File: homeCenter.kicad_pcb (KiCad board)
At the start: 2 copper layers, 59.7 x 57.1 mm, 45 parts, among them J1 sensor, J2 sensor, J3 mcu_en, J4 Conn_01x01_Male, P1 USB_C_Plug_USB2.0, Q1 S8050, U1 AMS1117-3.3, U2 ESP32-WROOM-32, U3 FengNiaoR3

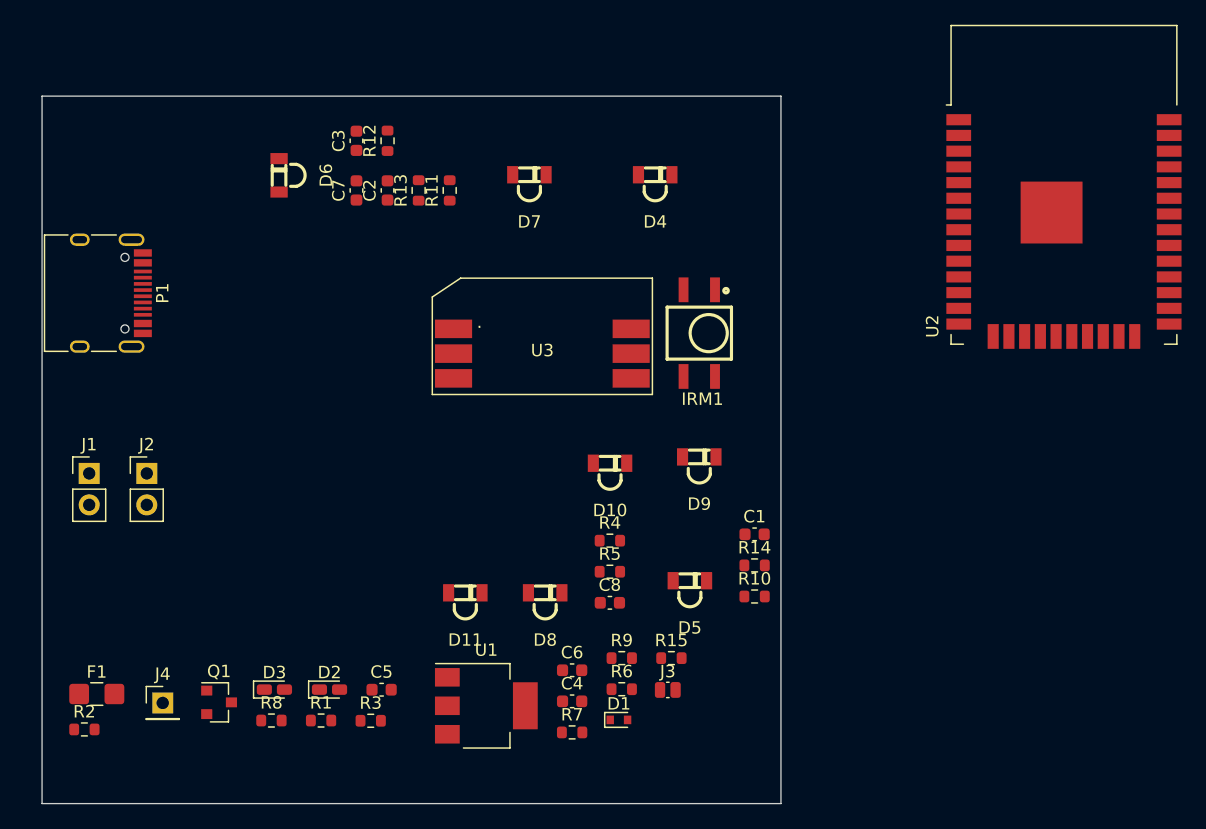
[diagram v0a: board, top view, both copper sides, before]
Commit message: convert to kicad 4.99
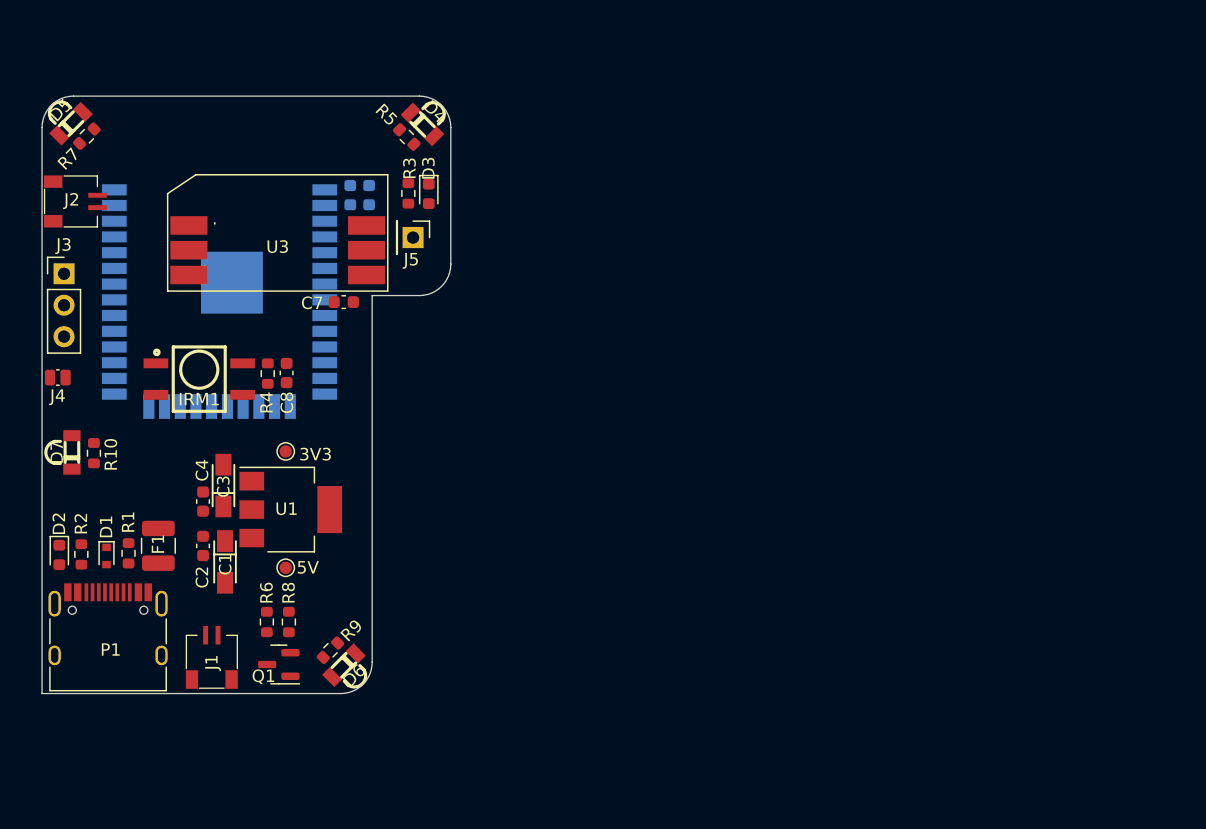
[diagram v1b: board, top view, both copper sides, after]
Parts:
- removed D10, D11, D8, D9: IR, kay:LED-SMD_L3.0-W2.7-RD
- removed R11: 1k, Resistor_SMD:R_0603_1608Metric
- removed R12, R14, R15: 47, Resistor_SMD:R_0603_1608Metric
- removed R13: 100k, Resistor_SMD:R_0603_1608Metric
- added 3V3: 3V3, TestPoint:TestPoint_Pad_D1.0mm, F.Cu at (45.1, 54.1)
- added 5V: 5V, TestPoint:TestPoint_Pad_D1.0mm, F.Cu at (45.1, 63.5)
- added J5: Conn_01x01_Male, kay:433M_ANT, F.Cu at (55.4, 36.8)
- C1, C3: footprint Capacitor_SMD:C_0603_1608Metric -> kay:CAP-SMD_L3.2-W1.6-RD
- C5, C6, U2: moved to B.Cu
- D2: value LED -> POWER; footprint LED_SMD:LED_0603_1608Metric_Castellated -> LED_SMD:LED_0603_1608Metric
- D3: value LED -> TEST; footprint LED_SMD:LED_0603_1608Metric_Castellated -> LED_SMD:LED_0603_1608Metric
- F1: footprint Fuse:Fuse_1206_3216Metric_Castellated -> Fuse:Fuse_1210_3225Metric
- J1, J2: footprint Connector_PinHeader_2.54mm:PinHeader_1x02_P2.54mm_Vertical -> kay:SH1.0MM-SMD
- J3: value mcu_en -> M_SERIAL; footprint Capacitor_SMD:C_0504_1310Metric_Pad0.83x1.28mm_HandSolder -> Connector_PinHeader_2.54mm:PinHeader_1x03_P2.54mm_Vertical
- J4: value Conn_01x01_Male -> mcu_en; footprint Connector_PinHeader_2.54mm:PinHeader_1x01_P2.54mm_Vertical -> Capacitor_SMD:C_0504_1310Metric_Pad0.83x1.28mm_HandSolder
- R1: value 51k -> NC/0
- R2: value NC/0 -> 47K
- R4: value 47K -> 100
- R5: value 100 -> 47
- R6: value 47 -> 1k
- R8: value 47 -> 100k
- moved U2 68.4 mm to (39.7, 41.2), turned to 180 degrees
- moved D5 62.1 mm to (27.7, 27.6), turned to -135 degrees
- moved R7 62.1 mm to (29.0, 28.6), turned to 45 degrees
- moved J3 59.2 mm to (27.2, 39.8)
- moved R10 54.6 mm to (29.6, 54.2), turned to 90 degrees
- moved D1 43.5 mm to (30.6, 62.5), turned to -90 degrees
- moved D7 43.2 mm to (27.8, 54.2), turned to -90 degrees
- moved C1 42.8 mm to (40.2, 63.0), turned to 90 degrees
- moved R3 42.7 mm to (55.0, 33.3), turned to 90 degrees
- moved C6 42.4 mm to (50.3, 33.4), turned to 90 degrees
- moved D3 41.9 mm to (56.6, 33.3), turned to -90 degrees
- moved IRM1 40.6 mm to (38.1, 48.3), turned to 90 degrees
- moved C5 40.0 mm to (51.8, 33.4), turned to 90 degrees
- moved D6 39.9 mm to (49.8, 71.4), turned to 45 degrees
- moved R5 38.8 mm to (54.9, 28.7), turned to -45 degrees
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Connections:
- J3 pad 1: /MCU_IO0 -> GND
- J3 pad 2: GND -> /MCU_RX0
- J4 pad 1: Net-(J4-Pad1) -> /MCU_IO0
- P1 pad A5: Net-(P1-PadA5) -> unconnected-(P1-PadA5)
- P1 pad A6: Net-(P1-PadA6) -> unconnected-(P1-PadA6)
- P1 pad A7: Net-(P1-PadA7) -> unconnected-(P1-PadA7)
- P1 pad B5: Net-(P1-PadA5) -> unconnected-(P1-PadB5)
- R1 pad 1: GND -> VCC
- R1 pad 2: Net-(P1-PadA5) -> Net-(F1-Pad2)
- R10 pad 1: Net-(D8-Pad2) -> Net-(D7-Pad2)
- R2 pad 1: VCC -> 3V3
- R2 pad 2: Net-(F1-Pad2) -> Net-(D2-Pad2)
- R3 pad 1: 3V3 -> Net-(D3-Pad2)
- R3 pad 2: Net-(D2-Pad2) -> 3V3
- R4 pad 1: Net-(D3-Pad2) -> Net-(C8-Pad1)
- R5 pad 1: Net-(C8-Pad1) -> Net-(D4-Pad2)
- R6 pad 1: Net-(D4-Pad2) -> /IR_TX0
- R6 pad 2: 3V3 -> Net-(Q1-Pad2)
- R8 pad 1: Net-(D6-Pad2) -> GND
- R8 pad 2: 3V3 -> Net-(Q1-Pad2)
- R9 pad 1: Net-(D7-Pad2) -> Net-(D6-Pad2)
- U2 pad 10: Net-(U2-Pad10) -> unconnected-(U2-Pad10)
- U2 pad 11: Net-(U2-Pad11) -> unconnected-(U2-Pad11)
- U2 pad 12: Net-(U2-Pad12) -> unconnected-(U2-Pad12)
- U2 pad 17: Net-(U2-Pad17) -> unconnected-(U2-Pad17)
- U2 pad 18: Net-(U2-Pad18) -> unconnected-(U2-Pad18)
- U2 pad 19: Net-(U2-Pad19) -> unconnected-(U2-Pad19)
- U2 pad 20: Net-(U2-Pad20) -> unconnected-(U2-Pad20)
- U2 pad 21: Net-(U2-Pad21) -> unconnected-(U2-Pad21)
- U2 pad 22: Net-(U2-Pad22) -> unconnected-(U2-Pad22)
- U2 pad 24: Net-(U2-Pad24) -> unconnected-(U2-Pad24)
- U2 pad 26: Net-(U2-Pad26) -> unconnected-(U2-Pad26)
- U2 pad 28: Net-(U2-Pad28) -> unconnected-(U2-Pad28)
- U2 pad 29: Net-(U2-Pad29) -> unconnected-(U2-Pad29)
- U2 pad 30: Net-(U2-Pad30) -> unconnected-(U2-Pad30)
- U2 pad 31: Net-(U2-Pad31) -> unconnected-(U2-Pad31)
- U2 pad 32: Net-(U2-Pad32) -> unconnected-(U2-Pad32)
- U2 pad 33: Net-(U2-Pad33) -> unconnected-(U2-Pad33)
- U2 pad 36: Net-(U2-Pad36) -> unconnected-(U2-Pad36)
- U2 pad 37: Net-(U2-Pad37) -> unconnected-(U2-Pad37)
- U2 pad 4: Net-(U2-Pad4) -> unconnected-(U2-Pad4)
- U2 pad 5: Net-(U2-Pad5) -> unconnected-(U2-Pad5)
- U2 pad 6: Net-(U2-Pad6) -> unconnected-(U2-Pad6)
- U2 pad 7: Net-(U2-Pad7) -> unconnected-(U2-Pad7)
- U2 pad 8: Net-(U2-Pad8) -> unconnected-(U2-Pad8)
- U2 pad 9: Net-(U2-Pad9) -> unconnected-(U2-Pad9)
- U3 pad 5: Net-(J4-Pad1) -> Net-(J5-Pad1)
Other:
- board size 59.7 x 57.1 mm -> 33 x 48.3 mm
- net class Default removed

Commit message: pcb
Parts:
- Q1: value S8050 -> Q_NPN_BEC
- moved R8 23.6 mm to (49.3, 44.6), turned to 0 degrees
- moved Q1 22.9 mm to (49.7, 49.0), turned to 0 degrees
- moved R6 22.3 mm to (49.3, 46.4), turned to 0 degrees
- moved C8 13.3 mm to (31.9, 47.2), turned to 90 degrees
- moved 5V1 12.9 mm to (32.6, 60.0)
- moved 3V1 12.5 mm to (49.1, 65.9)
- moved C4 11.9 mm to (45.7, 67.6), turned to 180 degrees
- moved C3 10.4 mm to (45.3, 65.8), turned to 0 degrees
- moved R4 10.3 mm to (33.4, 47.2), turned to 90 degrees
- moved C7 9.46 mm to (47.4, 32.9)
- moved J3 3.92 mm to (27.2, 43.7), turned to 180 degrees
- moved R10 2.98 mm to (27.7, 56.5), turned to -90 degrees
- moved C2 2.61 mm to (37.7, 64.2)
- moved U1 2.30 mm to (45.2, 61.1)
- moved U3 2.26 mm to (42.2, 38.0), turned to 180 degrees
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- renumbered 3V3 to 3V1, 5V to 5V1
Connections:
- J1 pad 2: /SENSOR0 -> /SENSOR1
- J2 pad 2: /SENSOR1 -> /SENSOR2
- Q1 pad 1: Net-(D4-Pad1) -> Net-(Q1-Pad1)
- Q1 pad 2: Net-(Q1-Pad2) -> GND
- Q1 pad 3: GND -> Net-(D4-Pad1)
- R6 pad 2: Net-(Q1-Pad2) -> Net-(Q1-Pad1)
- R8 pad 2: Net-(Q1-Pad2) -> Net-(Q1-Pad1)
- U2 pad 14: /433M_DAT -> unconnected-(U2-Pad14)
- U2 pad 16: /IR_RX0 -> unconnected-(U2-Pad16)
- U2 pad 23: /SENSOR0 -> unconnected-(U2-Pad23)
- U2 pad 26: unconnected-(U2-Pad26) -> /SENSOR1
- U2 pad 27: /SENSOR1 -> /IR_RX0
- U2 pad 36: unconnected-(U2-Pad36) -> /433M_DAT
- U2 pad 37: unconnected-(U2-Pad37) -> /SENSOR2
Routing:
- net Net-(D4-Pad1): track 0.00 -> 114.9 mm
- net 3V3: track 0.00 -> 95.7 mm, vias 0 -> 65
- net /SENSOR1: track 0.00 -> 29.0 mm, vias 0 -> 1
- net Net-(F1-Pad2): track 0.00 -> 11.4 mm
- net GND: track 0.00 -> 8.54 mm, vias 0 -> 17
- net Net-(J5-Pad1): track 0.00 -> 6.28 mm
- net /MCU_RX0: track 0.00 -> 5.34 mm
- net /IR_RX0: track 0.00 -> 5.32 mm, vias 0 -> 1
- net /MCU_TX0: track 0.00 -> 4.81 mm
- net /MCU_IO0: track 0.00 -> 4.49 mm, vias 0 -> 1
- net Net-(Q1-Pad1): track 0.00 -> 4.39 mm
- net /IR_TX0: track 0.00 -> 4.18 mm, vias 0 -> 1
- net VCC: track 0.00 -> 4.14 mm
- net /433M_DAT: track 0.00 -> 3.79 mm, vias 0 -> 1
- net Net-(C8-Pad1): track 0.00 -> 3.58 mm
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- added copper zone on B.Cu, net 3V3
- added copper zone on F.Cu, net 3V3
- added copper zone on B.Cu, net GND
- added copper zone on F.Cu, net GND
- added copper zone on F.Cu, net VCC
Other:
- outline, holes or cut-outs redrawn
- board text added: "2021.7"
- board text added: "Designed by Kay"
- board text added: "HomeCenter V0.2"

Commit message: v0.2
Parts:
- moved 5V 5.35 mm to (38.0, 60.4)
- renumbered 3V1 to 3V3, 5V1 to 5V
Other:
- board text added: "GND"
- board text added: "RX"
- board text added: "TX"
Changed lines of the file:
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@@
       (layerselection 0x00010fc_ffffffff)
       (disableapertmacros false)
-      (usegerberextensions false)
+      (usegerberextensions true)
       (usegerberattributes true)
       (usegerberadvancedattributes true)
-      (creategerberjobfile true)
+      (creategerberjobfile false)
       (svguseinch false)
       (svgprecision 6)
@@
       (plotinvisibletext false)
       (sketchpadsonfab false)
-      (subtractmaskfromsilk false)
+      (subtractmaskfromsilk true)
       (outputformat 1)
       (mirror false)
-      (drillshape 1)
+      (drillshape 0)
       (scaleselection 1)
-      (outputdirectory "")
+      (outputdirectory "gerber/")
     )
   )
@@
     (property "Sheetname" "")
     (attr through_hole)
-    (fp_text reference "C3" (at 0.071855 -0.018863) (layer "F.SilkS")
+    (fp_text reference "C3" (at -3.495294 0.0508) (layer "F.SilkS")
       (effects (font (size 1 1) (thickness 0.15)))
     )
@@
   )
   (footprint "TestPoint:TestPoint_Pad_D1.0mm" (layer "F.Cu")
-    (at 32.639 60.0325)
+    (at 37.973 60.3758)
     (descr "SMD pad as test Point, diameter 1.0mm")
     (tags "test point SMD pad")
@@
     (property "Sheetname" "")
     (attr exclude_from_pos_files)
-    (fp_text reference "5V1" (at 0 -1.651) (layer "F.SilkS")
+    (fp_text reference "5V" (at 0 1.6764) (layer "F.SilkS")
       (effects (font (size 1 1) (thickness 0.15)))
     )
@@
     (property "Sheetname" "")
     (attr through_hole)
-    (fp_text reference "D6" (at 0 1.193533 45) (layer "F.SilkS")
+    (fp_text reference "D6" (at -0.032974 1.311117 45) (layer "F.SilkS")
       (effects (font (size 1 1) (thickness 0.15)))
     )
@@
     (property "Sheetname" "")
     (attr exclude_from_pos_files)
-    (fp_text reference "3V1" (at 0 -1.524) (layer "F.SilkS")
+    (fp_text reference "3V3" (at 0 -1.524) (layer "F.SilkS")
       (effects (font (size 1 1) (thickness 0.15)))
     )
@@
     (property "Sheetname" "")
     (attr through_hole)
-    (fp_text reference "C1" (at -0.182194 0.044839 90) (layer "F.SilkS")
+    (fp_text reference "C1" (at 3.622294 -0.0258 90) (layer "F.SilkS")
       (effects (font (size 1 1) (thickness 0.15)))
     )
@@
     (property "Sheetname" "")
     (attr smd)
-    (fp_text reference "R1" (at 0.0255 -0.127 90) (layer "F.SilkS")
+    (fp_text reference "R1" (at -2.4506 0.0254 90) (layer "F.SilkS")
       (effects (font (size 1 1) (thickness 0.15)))
     )
@@
   (gr_line (start 52.065421 41.510949) (end 52.07 71.12) (layer "Edge.Cuts") (width 0.1))
   (gr_arc (start 55.88 27.94) (end 55.88 25.4) (angle 90) (layer "Edge.Cuts") (width 0.1))
+  (gr_text "GND" (at 30.0228 43.7642) (layer "F.SilkS")
+    (effects (font (size 1 1) (thickness 0.15)))
+  )
+  (gr_text "RX\n" (at 29.4386 41.2496) (layer "F.SilkS")
+    (effects (font (size 1 1) (thickness 0.15)))
+  )
+  (gr_text "TX" (at 29.4132 38.608) (layer "F.SilkS")
+    (effects (font (size 1 1) (thickness 0.15)))
+  )
   (gr_text "HomeCenter V0.2" (at 40.386 52.07) (layer "F.Mask")
     (effects (font (size 1.5 1.5) (thickness 0.15)))
